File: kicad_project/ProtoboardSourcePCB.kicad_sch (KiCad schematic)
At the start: 10 parts, among them J1 Conn_01x05, J2 Conn_01x05, J3 Conn_01x05, J4 Conn_01x05

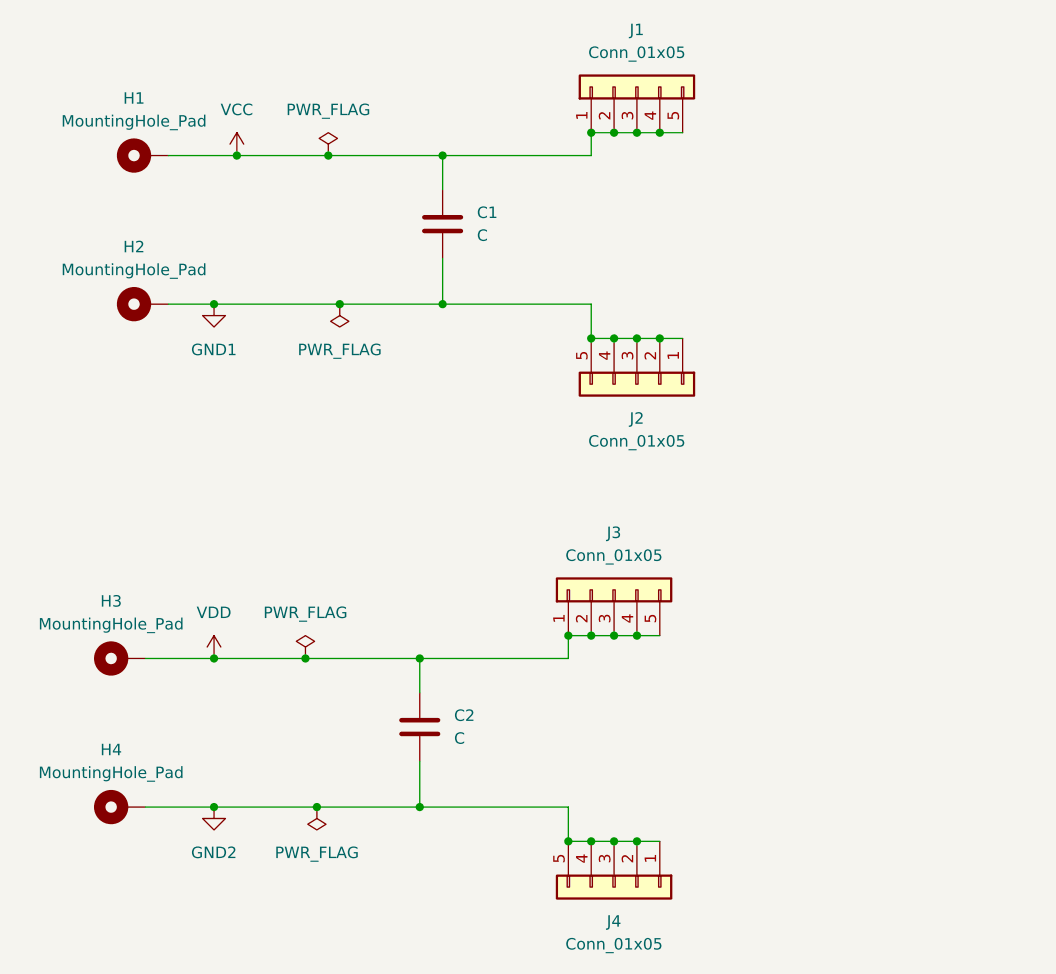
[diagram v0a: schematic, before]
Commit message: Corrigiendo huellas, colocando componentes y delimitando espacio de la PCB
Signed-off-by: RoMadrigal <rmadrigalmontes@gmail.com>
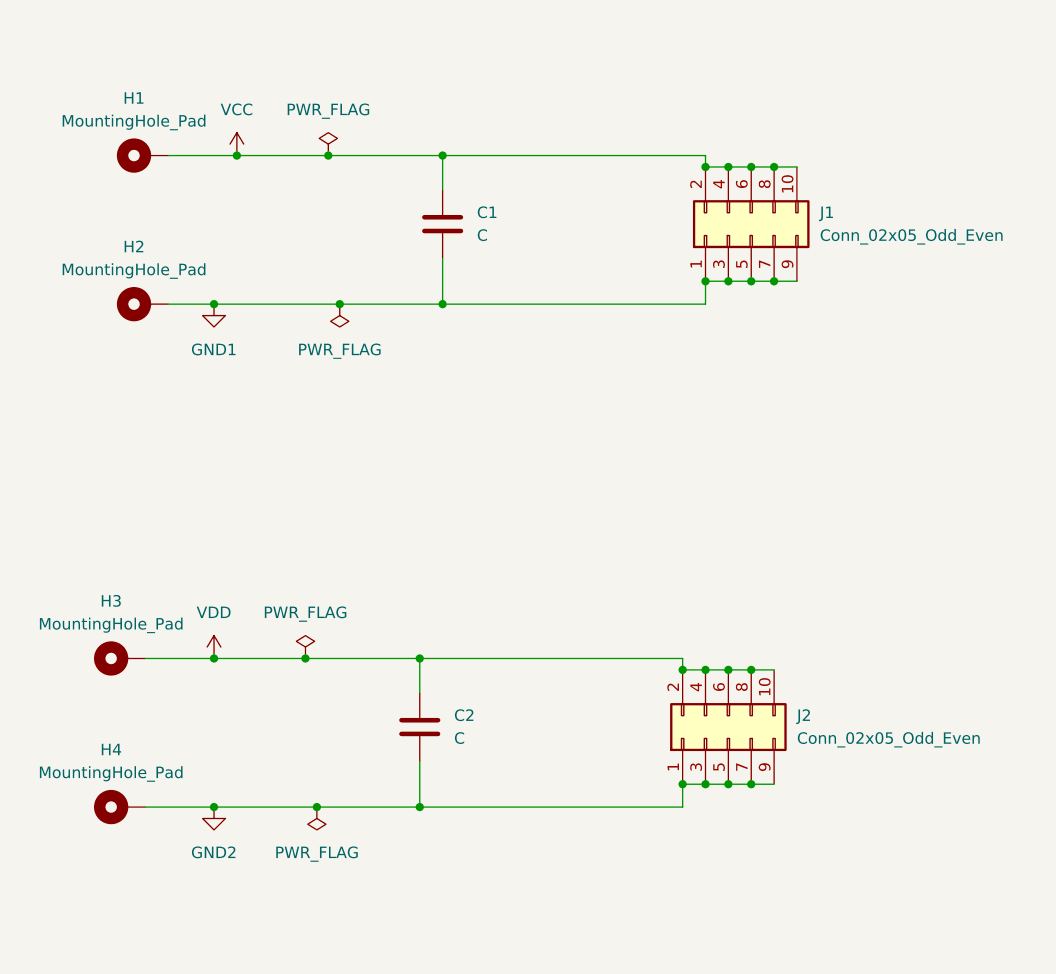
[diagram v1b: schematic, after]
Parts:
- removed J1, J2, J3, J4: Conn_01x05, Connector_PinHeader_2.54mm:PinHeader_1x05_P2.54mm_Vertical, symbol Connector_Generic:Conn_01x05
- added J1, J2: Conn_02x05_Odd_Even, Connector_PinHeader_2.54mm:PinHeader_2x05_P2.54mm_Vertical, symbol Connector_Generic:Conn_02x05_Odd_Even
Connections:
- net GND1: now also J1.1 (Pin_1), J1.3 (Pin_3), J1.5 (Pin_5), J1.7 (Pin_7), J1.9 (Pin_9)
- net GND2: now also J2.1 (Pin_1), J2.3 (Pin_3), J2.5 (Pin_5), J2.7 (Pin_7), J2.9 (Pin_9)
- net VCC: now also J1.10 (Pin_10), J1.2 (Pin_2), J1.4 (Pin_4), J1.6 (Pin_6), J1.8 (Pin_8)
- net VDD: now also J2.10 (Pin_10), J2.2 (Pin_2), J2.4 (Pin_4), J2.6 (Pin_6), J2.8 (Pin_8)

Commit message: Modificando huella de los capacitores y reacomodando componentes
Signed-off-by: RoMadrigal <rmadrigalmontes@gmail.com>
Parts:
- C1, C2: footprint Capacitor_THT:C_Disc_D5.0mm_W2.5mm_P2.50mm -> Capacitor_SMD:C_1206_3216Metric_Pad1.33x1.80mm_HandSolder
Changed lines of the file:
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@@
 			)
 		)
-		(property "Footprint" "Capacitor_THT:C_Disc_D5.0mm_W2.5mm_P2.50mm"
+		(property "Footprint" "Capacitor_SMD:C_1206_3216Metric_Pad1.33x1.80mm_HandSolder"
 			(at 82.2452 81.28 0)
 			(effects
@@
 			)
 		)
-		(property "Footprint" "Capacitor_THT:C_Disc_D5.0mm_W2.5mm_P2.50mm"
+		(property "Footprint" "Capacitor_SMD:C_1206_3216Metric_Pad1.33x1.80mm_HandSolder"
 			(at 79.7052 137.16 0)
 			(effects

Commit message: Modificando huellas de conector banana y reacomodando huella de C2
Signed-off-by: RoMadrigal <rmadrigalmontes@gmail.com>
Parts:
- H1, H2, H3, H4: footprint MountingHole:MountingHole_6.5mm_Pad -> MountingHole:MountingHole_6mm_Pad
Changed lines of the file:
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@@
 			)
 		)
-		(property "Footprint" "MountingHole:MountingHole_6.5mm_Pad"
+		(property "Footprint" "MountingHole:MountingHole_6mm_Pad"
 			(at 45.72 125.73 0)
 			(effects
@@
 			)
 		)
-		(property "Footprint" "MountingHole:MountingHole_6.5mm_Pad"
+		(property "Footprint" "MountingHole:MountingHole_6mm_Pad"
 			(at 45.72 142.24 0)
 			(effects
@@
 			)
 		)
-		(property "Footprint" "MountingHole:MountingHole_6.5mm_Pad"
+		(property "Footprint" "MountingHole:MountingHole_6mm_Pad"
 			(at 48.26 86.36 0)
 			(effects
@@
 			)
 		)
-		(property "Footprint" "MountingHole:MountingHole_6.5mm_Pad"
+		(property "Footprint" "MountingHole:MountingHole_6mm_Pad"
 			(at 48.26 69.85 0)
 			(effects
